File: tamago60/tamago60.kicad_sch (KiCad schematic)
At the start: 6 parts, among them J1 Conn_01x02_Female, SW1 SW_SPDT, SW600 JP19, U1 Pro_Micro

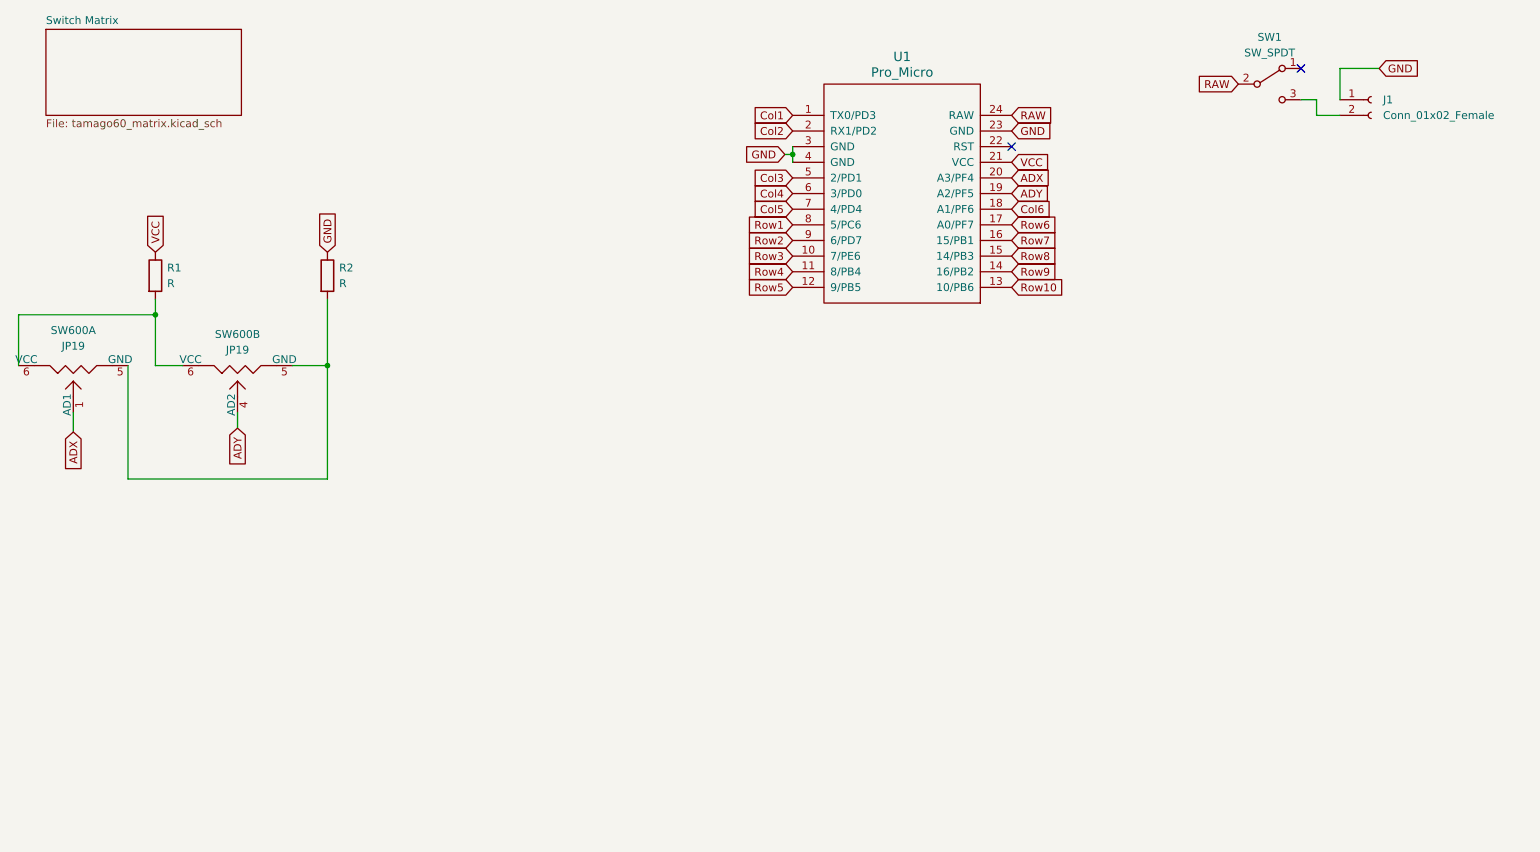
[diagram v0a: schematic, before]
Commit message: Finalize v1 design
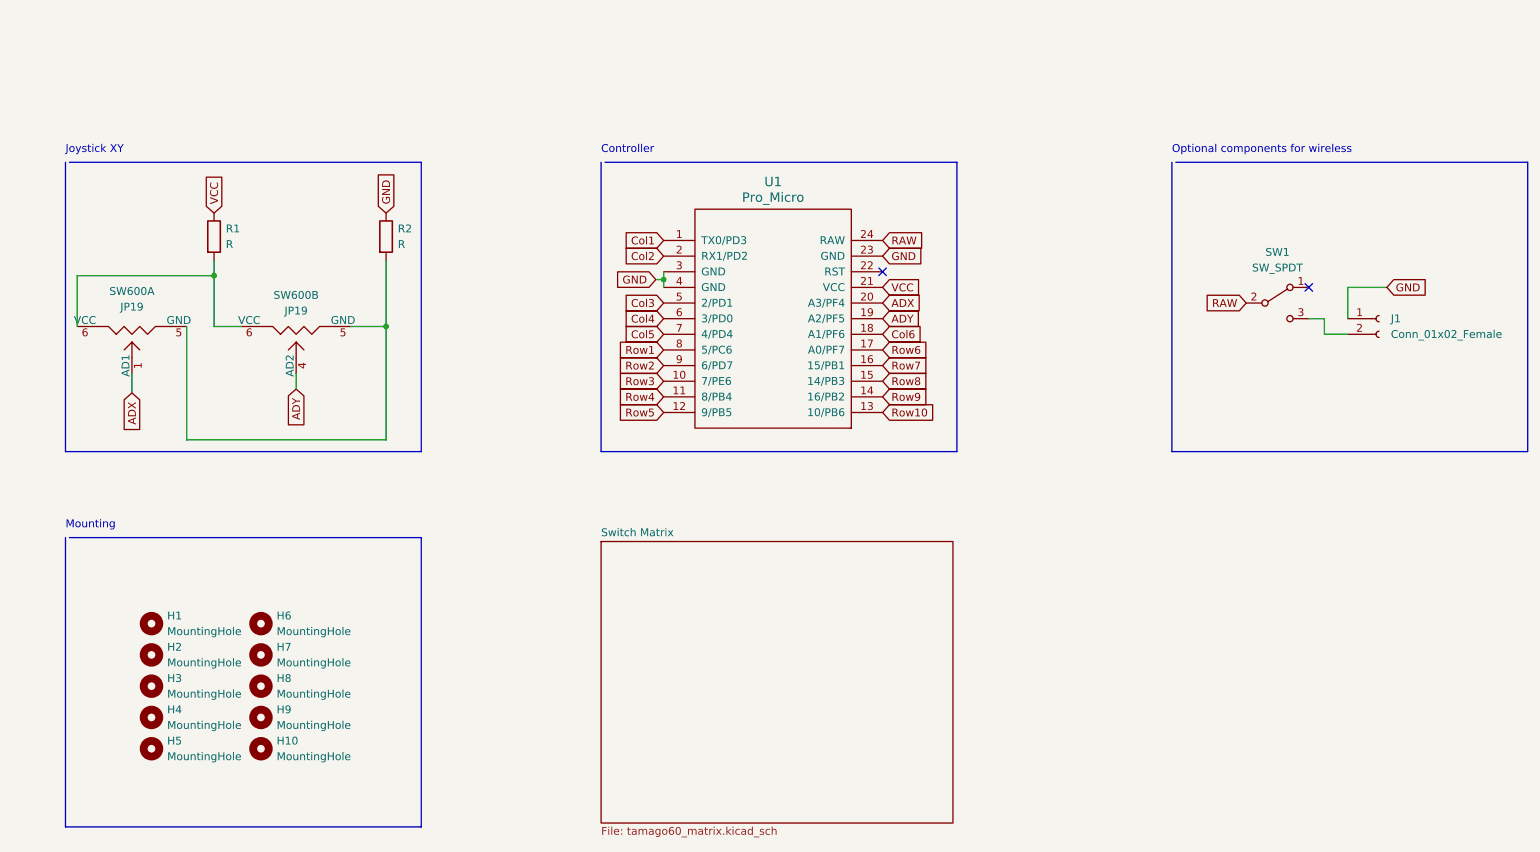
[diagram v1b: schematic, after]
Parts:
- added H1, H10, H2, H3, H4, H5, H6, H7, H8, H9: MountingHole, MountingHole:MountingHole_2.2mm_M2, symbol Mechanical:MountingHole
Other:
- note added: "Controller"
- note added: "Joystick XY"
- note added: "Mounting"
- note added: "Optional components for wireless"
- company: (none) -> EggsWorks, LLC
- title: (none) -> tamago60
- moved on the sheet: R1, R2, SW600A, SW600B, U1

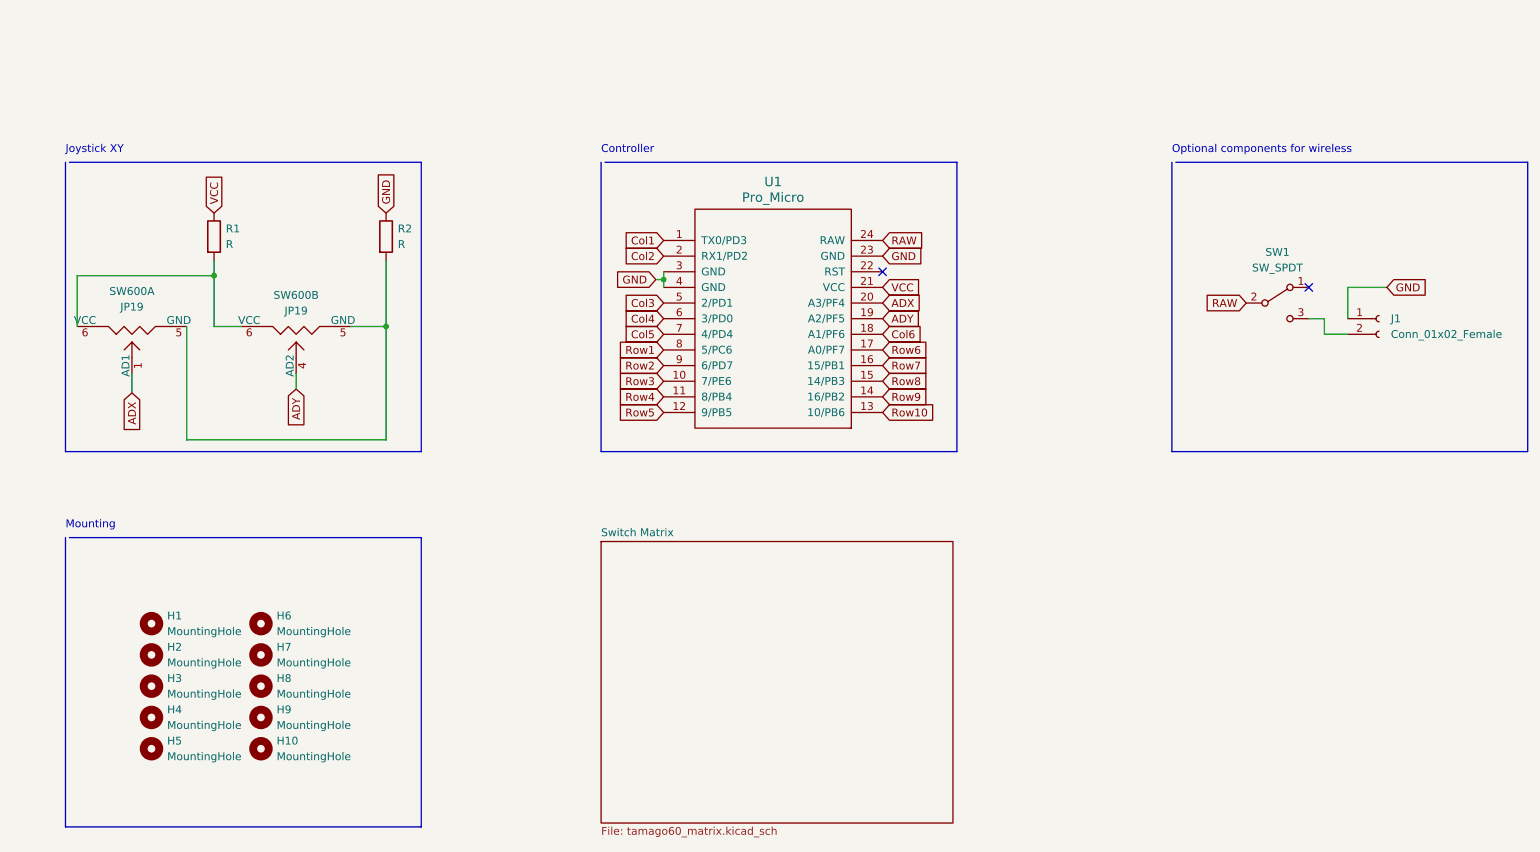
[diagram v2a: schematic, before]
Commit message: Replace JST with 2mm, move its position; update schematic to be consistent with PCB
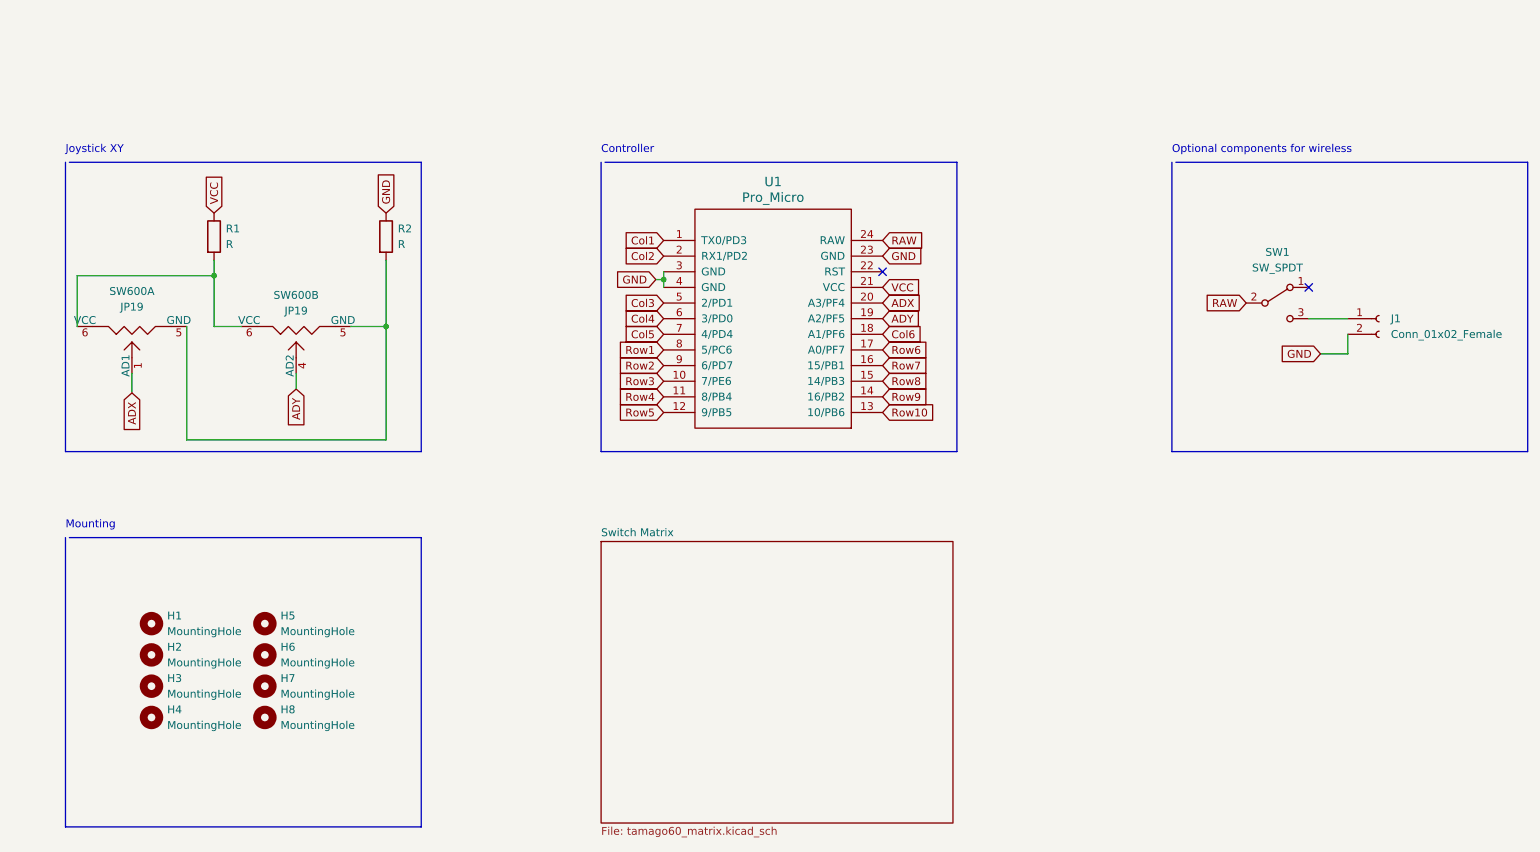
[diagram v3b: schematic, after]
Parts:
- removed H10, H9: MountingHole, MountingHole:MountingHole_2.2mm_M2, symbol Mechanical:MountingHole
- J1: footprint Connector_JST:JST_EH_S2B-EH_1x02_P2.50mm_Horizontal -> Connector_JST:JST_PH_S2B-PH-K_1x02_P2.00mm_Horizontal
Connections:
- net GND: now also J1.2 (Pin_2); no longer J1.1 (Pin_1)
- net at SW1.3 (C): now also J1.1 (Pin_1); no longer J1.2 (Pin_2)
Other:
- moved on the sheet: H5, H6, H7, H8

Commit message: Initial layout for tamago v2
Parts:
- removed H7, H8: MountingHole, MountingHole:MountingHole_2.2mm_M2, symbol Mechanical:MountingHole
- removed J1: Conn_01x02_Female, Connector_JST:JST_PH_S2B-PH-K_1x02_P2.00mm_Horizontal, symbol Connector:Conn_01x02_Female
- removed R1, R2: R, Resistor_SMD:R_1206_3216Metric, symbol Device:R
- removed SW1: SW_SPDT, Button_Switch_SMD:SW_SPDT_PCM12, symbol Switch:SW_SPDT
- removed SW600: JP19, tamago60:JP19, symbol tamago60:JP19
- removed U1: Pro_Micro, tamago60:ProMicro, symbol tamago60:Pro_Micro
- MH1: renamed from H1; footprint MountingHole:MountingHole_2.2mm_M2 -> tamago60:oval_mounting_hole
- MH2: renamed from H2; footprint MountingHole:MountingHole_2.2mm_M2 -> tamago60:circle_mounting_hole
- MH3: renamed from H3; footprint MountingHole:MountingHole_2.2mm_M2 -> tamago60:circle_mounting_hole_npth
- MH4: renamed from H4; footprint MountingHole:MountingHole_2.2mm_M2 -> tamago60:circle_mounting_hole
- MH5: renamed from H5; footprint MountingHole:MountingHole_2.2mm_M2 -> tamago60:circle_mounting_hole
- MH6: renamed from H6; footprint MountingHole:MountingHole_2.2mm_M2 -> tamago60:oval_mounting_hole
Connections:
- no-connect marks 2 -> 0
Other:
- added sheet MCU, USB, Power (tamago60_mcu.kicad_sch)
- note removed: "Controller"
- note removed: "Joystick XY"
- note removed: "Optional components for wireless"
- moved on the sheet: MH1, MH2, MH3, MH4, MH5, MH6
